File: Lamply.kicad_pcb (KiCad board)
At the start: 2 copper layers, 76.2 x 50.8 mm, 51 parts, among them P1 CONN_01X04, P2 CONN_01X04, P3 CONN_01X04, P4 CONN_01X04, P5 CONN_02X10, P7 CONN_01X04, P8 CONN_01X04, SW1 SETUP, SW2 RESET, U1 PAM2305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

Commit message: Simon overhaul assist
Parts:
- removed P5: CONN_02X10, particle:CONN-20-BIG
- removed W4, W6: TEST_1P, Measurement_Points:Measurement_Point_Square-SMD-Pad_Small
- added JP1: JUMPER, Oddities:NetTie-I, F.Cu at (195.2, 106.2)
- added W13: TCK, Measurement_Points:Measurement_Point_Square-SMD-Pad_Small, F.Cu at (186.8, 95.2)
- added W16: TRST, Measurement_Points:Measurement_Point_Square-SMD-Pad_Small, F.Cu at (196.0, 95.2)
- added W17: gND, Measurement_Points:Measurement_Point_Square-SMD-Pad_Small, F.Cu at (198.2, 103.8)
- added W8: 3V3, Measurement_Points:Measurement_Point_Square-SMD-Pad_Small, F.Cu at (196.5, 80.0)
- W11: value TEST_1P -> JTAG_RST
- W12: value TEST_1P -> TDO
- W14: value TEST_1P -> TMS
- W15: value TEST_1P -> TDI
- moved W12 35.3 mm to (192.8, 95.2)
- moved P1 28.2 mm to (225.0, 72.8), turned to 180 degrees
- moved P2 17.6 mm to (225.0, 81.5), turned to 180 degrees
- moved W14 14.6 mm to (192.5, 99.5)
- moved P3 13.4 mm to (225.0, 89.5), turned to 180 degrees
- moved R1 12.9 mm to (211.2, 72.8)
- moved W11 12.0 mm to (195.5, 75.2)
- moved R4 11.1 mm to (211.0, 89.5)
- moved C11 9.93 mm to (186.8, 102.8), turned to 90 degrees
- moved W15 9.45 mm to (189.8, 95.2)
- moved R3 8.70 mm to (186.8, 76.5), turned to 90 degrees
- moved W10 8.64 mm to (170.8, 74.5)
- moved R2 8.30 mm to (211.2, 81.5)
- moved W3 7.76 mm to (209.5, 86.8)
- moved R8 7.66 mm to (192.5, 81.2), turned to 0 degrees
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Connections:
- C1 pad 2: GND -> GNDA
- C10 pad 2: GND -> GNDA
- C11 pad 2: GND -> GNDA
- C2 pad 2: GND -> GNDA
- C3 pad 2: GND -> GNDA
- C4 pad 2: GND -> GNDA
- C5 pad 2: GND -> GNDA
- C6 pad 2: GND -> GNDA
- C7 pad 2: GND -> GNDA
- C8 pad 2: GND -> GNDA
- C9 pad 2: GND -> GNDA
- D3 pad 1: GND -> GNDA
- P1 pad 1: /UVCC -> GND
- P1 pad 2: Net-(P1-Pad2) -> /UVCC
- P1 pad 4: GND -> Net-(P1-Pad4)
- P2 pad 1: /UVCC -> GND
- P2 pad 2: Net-(P1-Pad3) -> /UVCC
- P2 pad 4: GND -> Net-(P1-Pad3)
- P3 pad 1: /UVCC -> GND
- P3 pad 2: Net-(P2-Pad3) -> /UVCC
- P3 pad 4: GND -> Net-(P2-Pad3)
- P4 pad 1: /UVCC -> GND
- P4 pad 2: Net-(P3-Pad3) -> /UVCC
- P4 pad 4: GND -> Net-(P3-Pad3)
- P7 pad 1: /UVCC -> GND
- P7 pad 2: Net-(P4-Pad3) -> /UVCC
- P7 pad 4: GND -> Net-(P4-Pad3)
- R1 pad 1: Net-(P1-Pad2) -> Net-(P1-Pad4)
- R1 pad 2: /D0 -> /D2
- R4 pad 1: /D2 -> /D0
- U1 pad 2: GND -> GNDA
- U2 pad 1: GND -> GNDA
- U2 pad 13: GND -> GNDA
- U2 pad 15: GND -> GNDA
- U2 pad 25: GND -> GNDA
- U2 pad 28: GND -> GNDA
- U2 pad 37: GND -> GNDA
- U2 pad 39: GND -> GNDA
- U2 pad 4: GND -> GNDA
- U2 pad 59: GND -> GNDA
- U2 pad 6: GND -> GNDA
- U2 pad 65: GND -> GNDA
- U2 pad 66: GND -> GNDA
- U2 pad 67: GND -> GNDA
- U2 pad 68: GND -> GNDA
- U2 pad 69: GND -> GNDA
- U2 pad 70: GND -> GNDA
- U2 pad 71: GND -> GNDA
- U2 pad 72: GND -> GNDA
- U2 pad 73: GND -> GNDA
- W11 pad 1: Net-(D2-Pad4) -> /JTAG_RST
- W12 pad 1: /A0 -> /TDO
- W14 pad 1: Net-(D2-Pad3) -> /TMS
- W15 pad 1: Net-(D2-Pad2) -> /TDI
- W3 pad 1: /D2 -> /D0
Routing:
- net GND: track 452.1 -> 178.3 mm
- net GNDA: track 0.00 -> 194.1 mm, vias 0 -> 2
- net /UVCC: track 154.2 -> 97.2 mm, vias 1 -> 0
- net /JTAG_RST: track 59.4 -> 17.9 mm, vias 3 -> 0
- net /TCK: track 62.5 -> 29.0 mm
- net /TRST: track 83.3 -> 56.3 mm, vias 3 -> 2
- net /TMS: track 60.6 -> 37.4 mm, vias 4 -> 2
- net /D0: track 20.4 -> 43.5 mm
- net /TDI: track 54.8 -> 31.8 mm
- net +3V3: track 120.1 -> 103.1 mm, vias 3 -> 0
- net /A0: track 12.4 -> 0.00 mm, vias 2 -> 0
- net /TDO: track 66.7 -> 55.9 mm
- net /A1: track 12.2 -> 2.54 mm
- net /RGB_G: track 20.4 -> 10.9 mm
- net Net-(P1-Pad3): track 23.8 -> 14.7 mm
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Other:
- net class Default: clearance 0.2 -> 0.254; trace_width 0.4 -> 0.254
- net class Power added: clearance 0.254, trace_width 0.254, via_dia 0.6, via_drill 0.4
- rule trace_clearance: 0.2 -> 0.254
- rule trace_min: 0.4 -> 0.254

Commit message: Enlarging via drills
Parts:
- moved P1 7.75 mm to (217.2, 72.8)
- moved P2 7.75 mm to (217.2, 81.5)
- moved P3 7.75 mm to (217.2, 89.5)
- moved P4 7.75 mm to (217.2, 97.5)
- moved P7 7.75 mm to (217.2, 105.5)
- moved R1 7.54 mm to (203.8, 72.0)
- moved R6 7.35 mm to (203.9, 101.5)
- moved R2 6.25 mm to (205.2, 79.8), turned to 270 degrees
- moved R5 5.95 mm to (205.2, 96.8), turned to 270 degrees
- moved R4 5.88 mm to (205.2, 88.2), turned to 270 degrees
- moved W7 5.71 mm to (200.2, 99.2)
- moved W3 5.06 mm to (205.2, 84.0)
- moved W5 5.03 mm to (205.2, 92.5)
- moved W1 4.83 mm to (205.2, 75.8)
- moved R10 1.96 mm to (190.4, 99.5)
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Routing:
- net GND: track 178.3 -> 162.8 mm
- net /D2: track 46.3 -> 38.5 mm
- net /UVCC: track 97.2 -> 89.8 mm
- net /TDO: track 55.9 -> 48.6 mm
- net Net-(P7-Pad3): track 16.1 -> 9.14 mm
- net /D1: track 41.9 -> 35.2 mm
- net /D0: track 43.5 -> 38.4 mm
- net /TRST: track 56.3 -> 51.5 mm
- net Net-(P4-Pad3): track 16.1 -> 13.9 mm
- net /TMS: track 37.4 -> 38.4 mm
- net /TCK: track 29.0 -> 28.3 mm
- net Net-(P2-Pad3): track 14.2 -> 13.6 mm

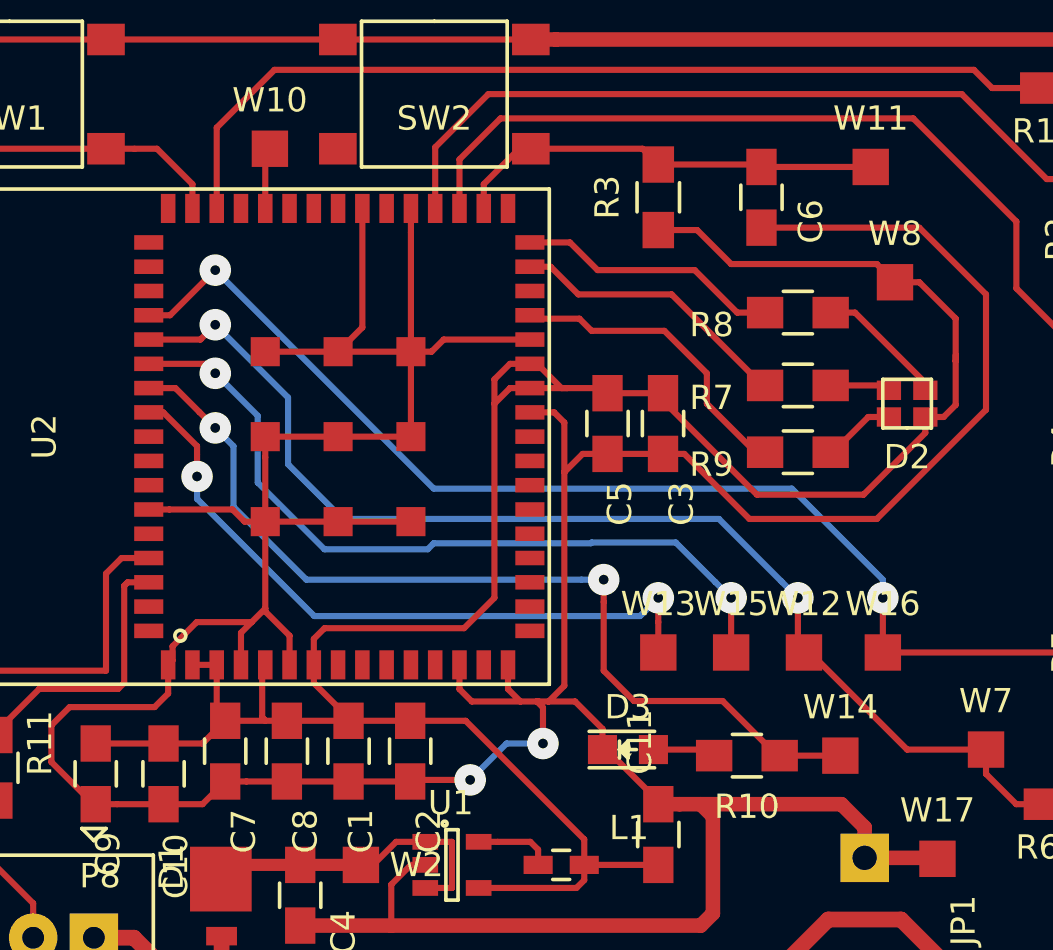
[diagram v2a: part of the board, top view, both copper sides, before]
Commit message: Enlarging vias
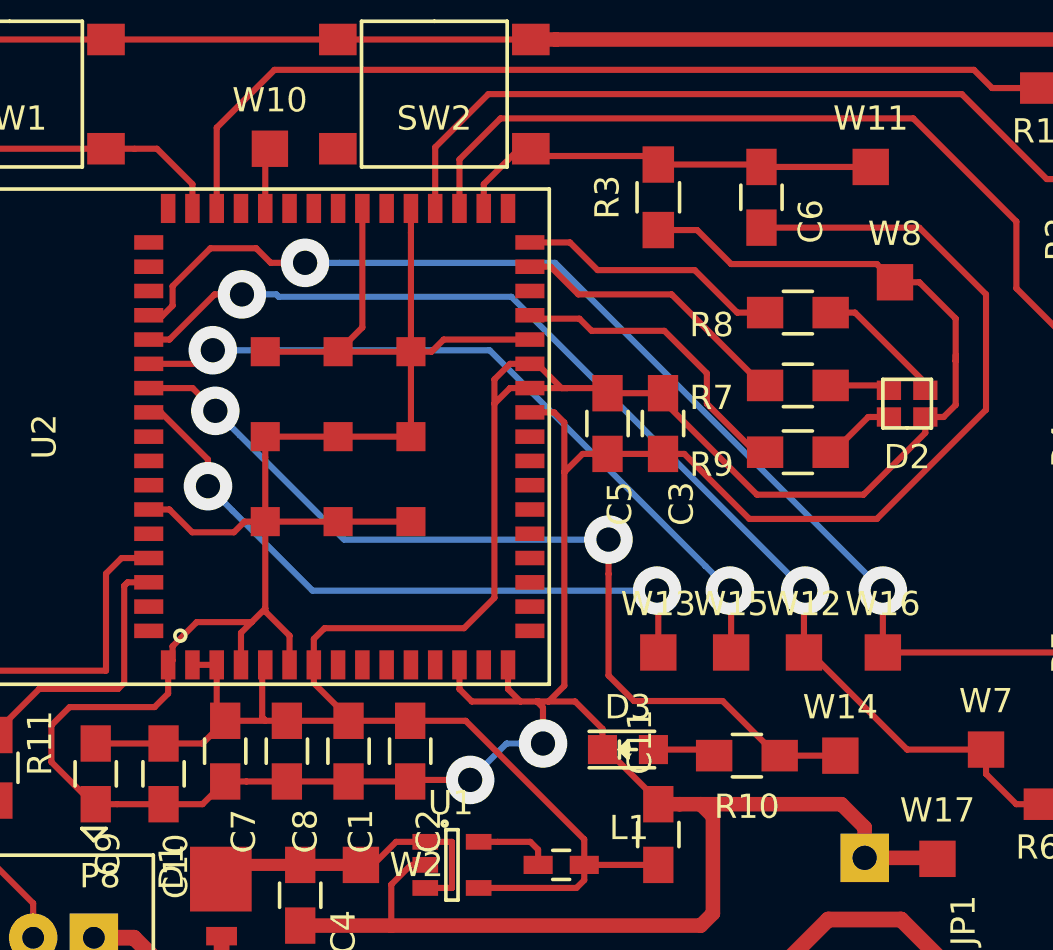
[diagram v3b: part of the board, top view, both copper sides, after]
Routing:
- net /TDI: track 32.1 -> 30.8 mm
- net /TCK: track 28.3 -> 27.2 mm
- net /TRST: track 51.5 -> 52.2 mm
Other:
- net class Default: via_dia 0.6 -> 2; via_drill 0.4 -> 1
